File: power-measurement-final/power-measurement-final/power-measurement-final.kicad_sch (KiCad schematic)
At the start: 75 parts, among them J10 Conn_01x01_Pin, J11 Conn_01x02_Pin, J12 Conn_01x01_Pin, J13 Conn_01x01_Pin, J2 Conn_01x02_Socket, J3 Conn_01x03_Socket, J4 Conn_01x07_Socket, J5 Conn_01x07_Socket, J6 Conn_01x05_Socket, J7 RFShield_OnePiece, J8 Conn_01x03_Socket, J9 Conn_01x01_Pin, U3 CNY17-3

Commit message: Small changes
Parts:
- added C?: 100n, Capacitor_SMD:C_1206_3216Metric_Pad1.33x1.80mm_HandSolder, symbol Power-Analyzer-rescue:C_Small
- added C?: 10u, Capacitor_SMD:C_1206_3216Metric_Pad1.33x1.80mm_HandSolder, symbol Power-Analyzer-rescue:CP_Small
- added D5: D_Zener_Small, symbol Device:D_Zener_Small
- added F1: B72214S0551K101, symbol Device:Fuse_Small
- added R27: 6.8, Resistor_THT:R_Radial_Power_L12.0mm_W8.0mm_P5.00mm, symbol Device:R_Small
- added RV1: B72214S0551K101, Resistor_THT:R_Axial_DIN0204_L3.6mm_D1.6mm_P7.62mm_Horizontal, symbol Device:Varistor
- added U5: ~, Power_Supply:RS_2333523, symbol Power_Supply:RS_2333523
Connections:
- net +5V: now also C?.1, C?.1, D5.1 (K), U5.
- net GND: now also C?.2, C?.2, D5.2 (A), U5.
- net GNDD: now also RV1.2, U5.
- net HIGH_in: now also F1.2
- new net: R27.2, U5.
- new net: F1.1, R27.1, RV1.1

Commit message: SMPS routed
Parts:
- removed F1: B72214S0551K101, symbol Device:Fuse_Small
- removed R13: 1k, Resistor_SMD:R_1206_3216Metric, symbol Device:R_Small
- removed TP4: TestPoint, TestPoint:TestPoint_Plated_Hole_D3.0mm, symbol Connector:TestPoint
- removed U3: CNY17-3, Package_DIP:DIP-6_W7.62mm_LongPads, symbol Isolator:CNY17-3
- added U6: ADuM1250, Package_SO:SO-8_5.3x6.2mm_P1.27mm, symbol Isolator:ADuM1250
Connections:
- net +5V: now also U5.6, U6.1 (VDD1); no longer U5.
- net 3V3D: now also U6.8 (VDD2)
- net GND: now also U5.4, U6.4 (GND1); no longer U5.
- net GNDD: now also U5.2 (AC_input), U6.5 (GND2); no longer U5.
- net HIGH_in: now also R27.1, RV1.1
- net SCL/XDIR/PB0: now also U6.2 (SDA1)
- net at R27.2: now also U5.1 (AC_input); no longer U5.
- net at R?.2: now also U6.6 (SCL2)
- no-connect marks 8 -> 9
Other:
- moved on the sheet: R?

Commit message: updates
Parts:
- removed R?: 10k, Potentiometer_THT:Potentiometer_ACP_CA9-V10_Vertical_Hole, symbol Device:R_Variable
- added RV2: R_Potentiometer, Potentiometer_THT:Potentiometer_ACP_CA9-V10_Vertical_Hole, symbol Device:R_Potentiometer
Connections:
- net voltage_pos: now also RV2.2
- net at R?.2: now also RV2.1
- no-connect marks 9 -> 10

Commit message: power rmeasurement final finished
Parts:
- removed D3, D4: D_Schottky, symbol Device:D_Schottky
- added TP4: TestPoint, TestPoint:TestPoint_Plated_Hole_D3.0mm, symbol Connector:TestPoint
- D5: footprint (none) -> Diode_SMD:D_1206_3216Metric_Pad1.42x1.75mm_HandSolder
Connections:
- no-connect marks 10 -> 11
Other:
- note added: "5V Jumper"
- note added: "GND Jumper"
- note added: "Netzeil"
- note added: "Optokoppler"
- moved on the sheet: C?, D5, D?, FB?, J10, J11, J12, J13, J2, J3, J4, J5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

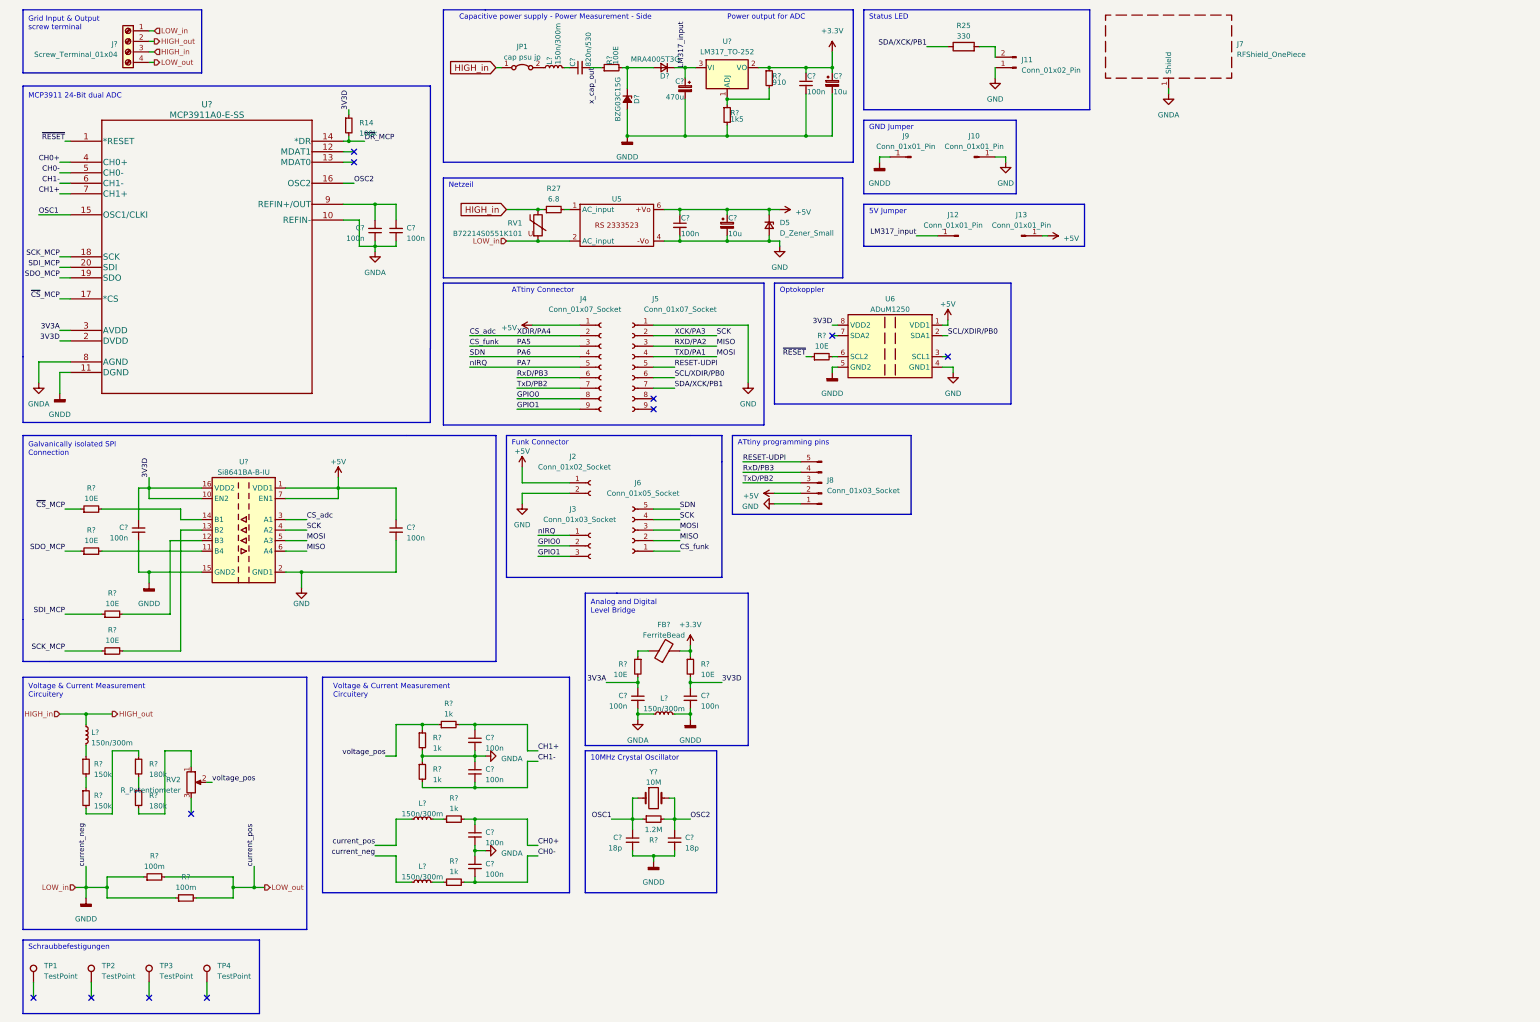
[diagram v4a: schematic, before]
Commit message: Updated power measurement
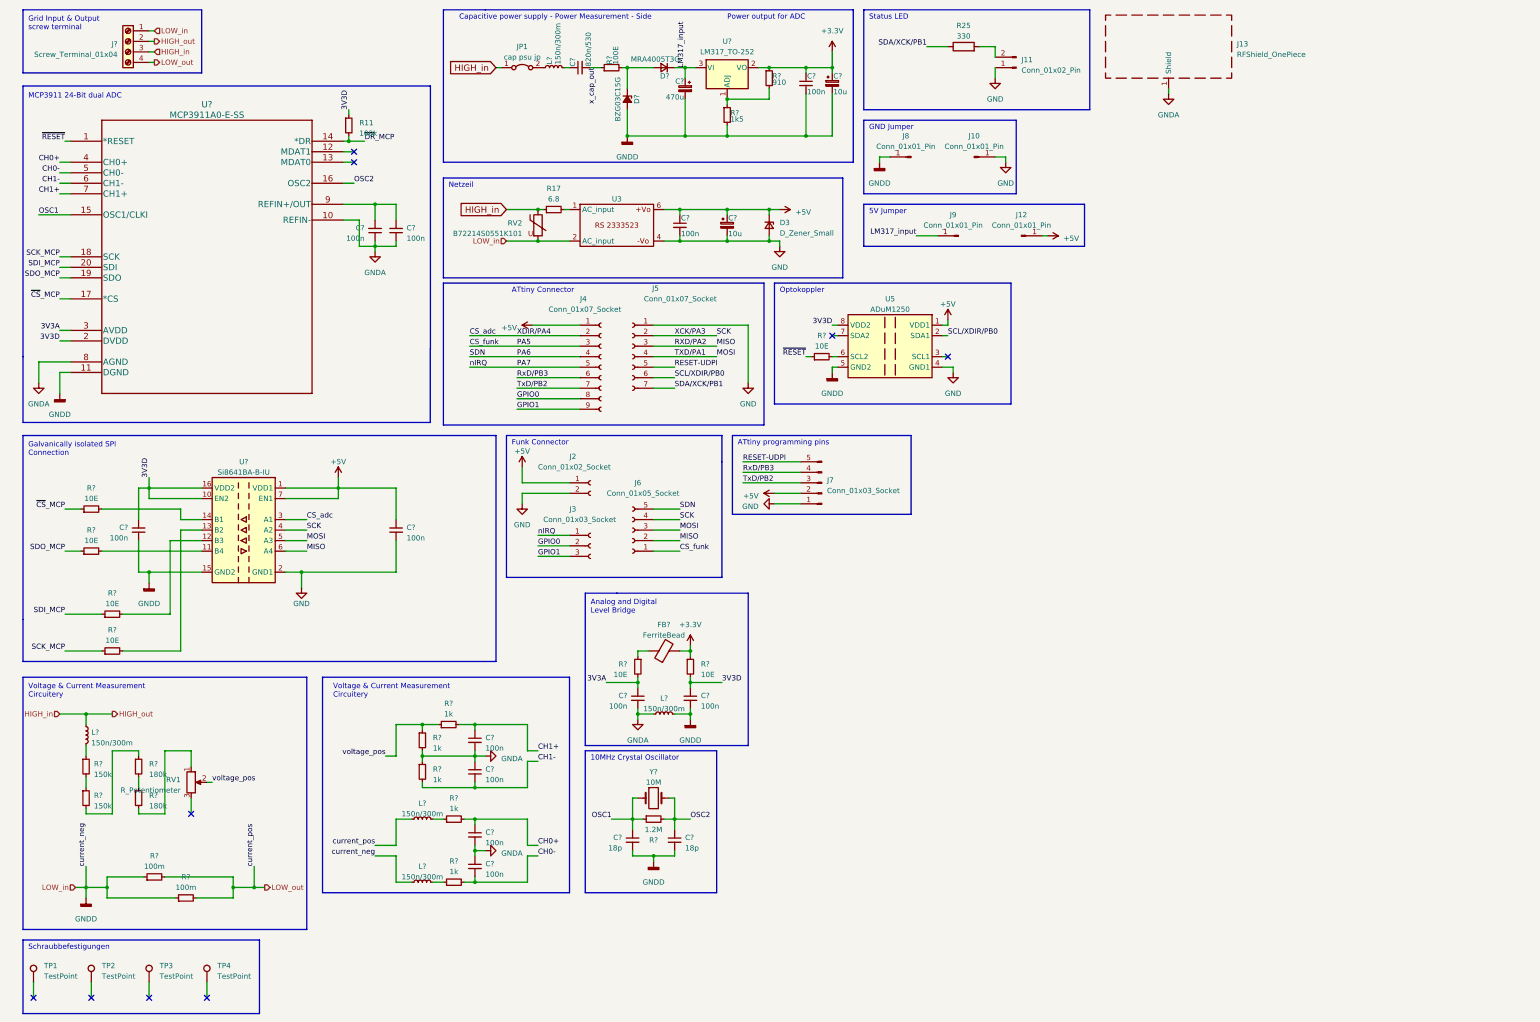
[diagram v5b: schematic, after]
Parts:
- J5: symbol Connector:Conn_01x09_Socket -> Connector:Conn_01x07_Socket
- renumbered D5 to D3, J13 to J12, J7 to J13, J8 to J7, J9 to J8, J12 to J9, R14 to R11, R27 to R17, RV2 to RV1, RV1 to RV2, U5 to U3, U6 to U5
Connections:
- no-connect marks 11 -> 9
